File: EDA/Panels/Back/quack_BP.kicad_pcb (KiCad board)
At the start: 2 copper layers, 60 x 22.8 mm, 3 parts

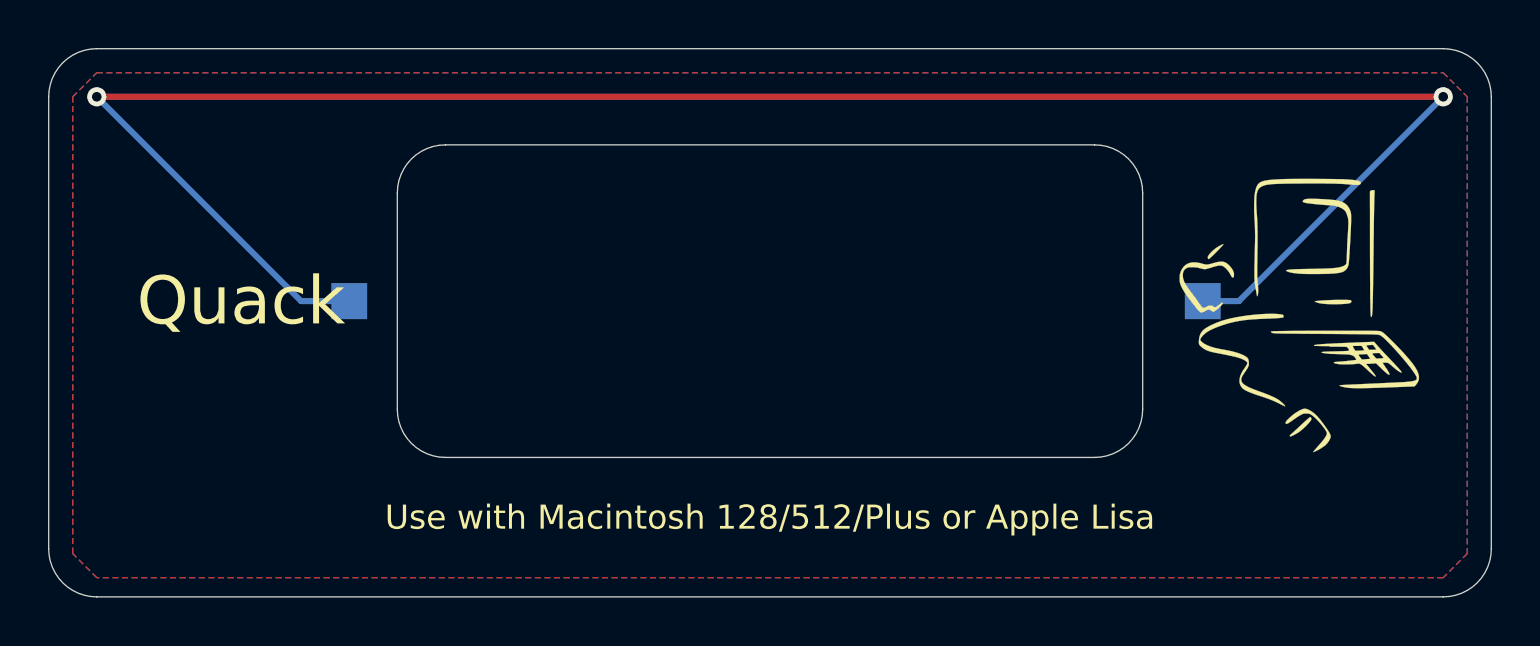
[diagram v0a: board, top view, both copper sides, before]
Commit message: Back panel update: Apple IIc
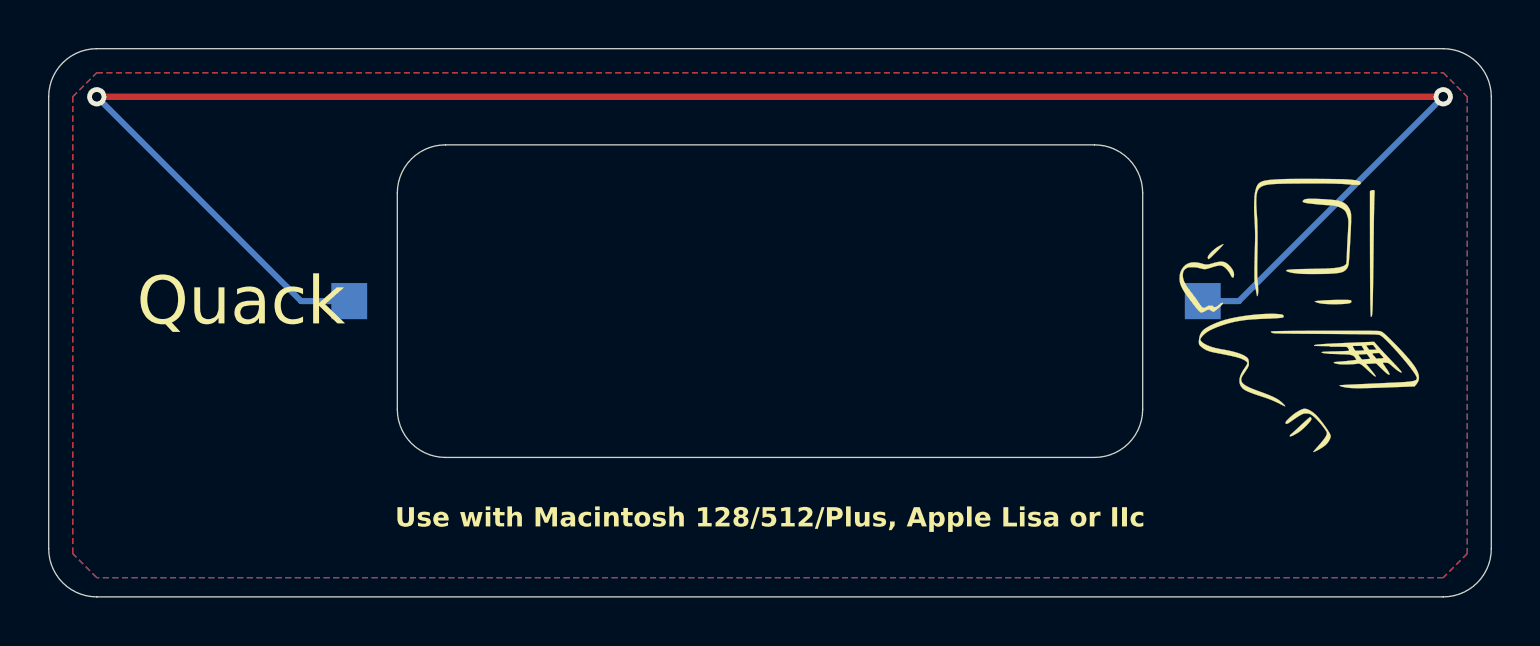
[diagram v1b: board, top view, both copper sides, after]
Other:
- net class Default removed
- board text added: "Use with Macintosh 128/512/Plus, Apple Lisa or IIc"
- board text removed: "Use with Macintosh 128/512/Plus or Apple Lisa"
